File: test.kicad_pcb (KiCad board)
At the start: 2 copper layers, 161 parts, among them Q1 T2N7002AK, Q2 T2N7002AK, SW1 SW_Push, U1 ESP32-S3-WROOM-1, U2 LD1117S33TR_SOT223, U3 SN75176AD, U4 LM321, U5 LM321

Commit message: final placement-no route
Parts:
- L1, U4, U5, c4, c5, dz1, dz2, jadc1, jadc2, ra1, ra2, ra3, ra4, ra5, ra6: moved to F.Cu
- cf1, flash1, rf1, rf2, rms1: moved to B.Cu
- moved 220in1 103.9 mm to (96.8, 97.0), turned to 180 degrees
- moved MODBUS1 42.8 mm to (6.30, 35.2), turned to -90 degrees
- moved aco2 28.8 mm to (26.5, 61.7)
- moved r18 28.8 mm to (27.8, 54.3)
- moved r20 28.8 mm to (25.2, 54.2)
- moved r22 28.8 mm to (26.3, 68.4)
- moved cr2 26.3 mm to (35.0, 56.6)
- moved cb1 22.2 mm to (50.0, 57.1)
- moved cm3 22.2 mm to (59.7, 57.4)
- moved cm1 22.2 mm to (65.7, 57.4)
- moved cm2 22.2 mm to (62.7, 57.4)
- moved cm4 22.2 mm to (56.7, 57.4)
- moved cm5 22.2 mm to (53.7, 57.4)
- moved bridge2 21.3 mm to (62.6, 66.5)
- moved rb2 21.3 mm to (49.2, 64.3)
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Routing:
- net /ESP_GPIO_0: track 66.8 -> 0.00 mm
- net MGND: track 59.4 -> 0.00 mm
- net /RS485_B: track 26.5 -> 0.00 mm
- net /RS485_AO: track 23.2 -> 0.00 mm
- net /+3.3V: track 20.4 -> 0.00 mm
- net /RS485_BO: track 20.4 -> 0.00 mm
- net Net-(mcu1-PC14): track 17.2 -> 0.00 mm
- net Net-(U1-IO3): track 17.0 -> 0.00 mm, vias 1 -> 0
- net /+M5V: track 16.6 -> 0.00 mm, vias 1 -> 0
- net /RS485_A: track 15.5 -> 0.00 mm
- net Net-(mcu1-PC13): track 14.8 -> 0.00 mm
- net Net-(mcu1-PF1): track 13.8 -> 0.00 mm
- net /ESP_EN: track 13.4 -> 0.00 mm
- net /DO4: track 13.2 -> 0.00 mm
- net /RESET: track 12.9 -> 0.00 mm, vias 1 -> 0
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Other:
- board outline added: 100 x 100 mm

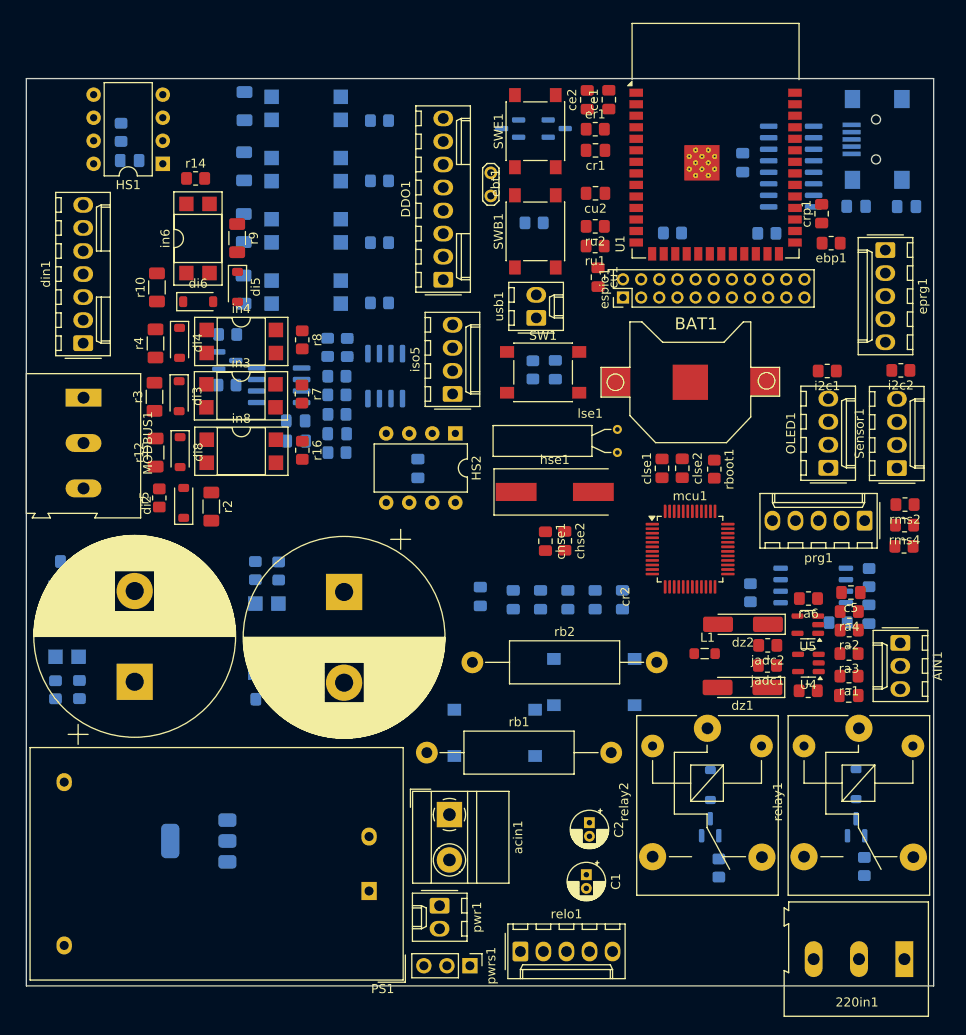
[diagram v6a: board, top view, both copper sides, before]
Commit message: except DI1-4 all other logics are ok
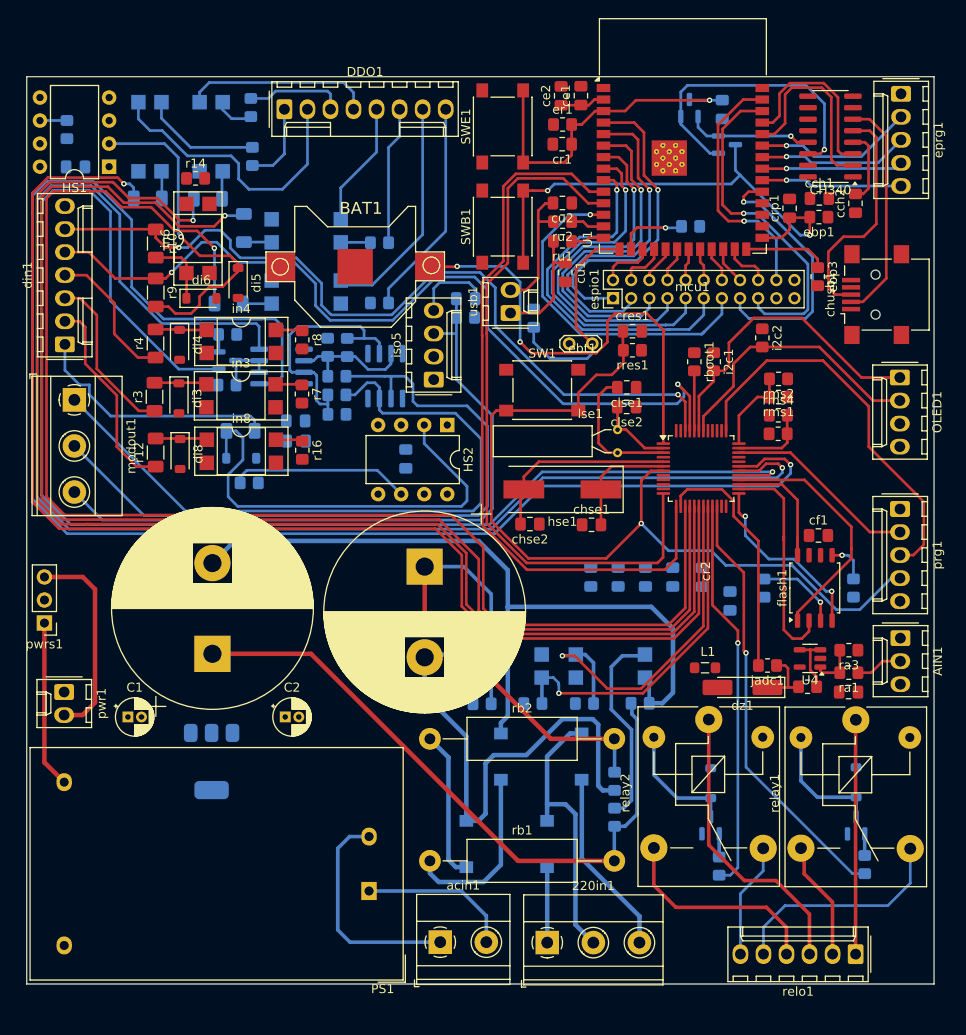
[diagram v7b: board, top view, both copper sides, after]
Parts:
- removed MODBUS1: Screw_Terminal_01x03, TerminalBlock:TerminalBlock_Altech_AK300-3_P5.00mm
- removed Sensor1: Conn_01x04_Pin, Connector_Molex:Molex_KK-254_AE-6410-04A_1x04_P2.54mm_Vertical
- removed U5: LM321, Package_TO_SOT_SMD:SOT-23-5
- removed c5: 100nF, Capacitor_SMD:C_0805_2012Metric_Pad1.18x1.45mm_HandSolder
- removed dz2: D_Zener, Diode_SMD:D_MiniMELF_Handsoldering
- removed jadc2: 0, Resistor_SMD:R_0805_2012Metric_Pad1.20x1.40mm_HandSolder
- removed ra2: 68K, Resistor_SMD:R_0805_2012Metric_Pad1.20x1.40mm_HandSolder
- removed ra4: 33K, Resistor_SMD:R_0805_2012Metric_Pad1.20x1.40mm_HandSolder
- removed ra6: 68, Resistor_SMD:R_0805_2012Metric_Pad1.20x1.40mm_HandSolder
- added modout1: Screw_Terminal_01x03, TerminalBlock_Phoenix:TerminalBlock_Phoenix_MKDS-1,5-3-5.08_1x03_P5.08mm_Horizontal, F.Cu at (5.29, 35.4)
- 220in1: footprint TerminalBlock:TerminalBlock_Altech_AK300-3_P5.00mm -> TerminalBlock_Phoenix:TerminalBlock_Phoenix_MKDS-1,5-3-5.08_1x03_P5.08mm_Horizontal
- CH340, cch1, cch2, cf1, chusb1, cres1, ebp3, flash1, rms1, rres1: moved to F.Cu
- acin1: footprint TerminalBlock_MetzConnect:TerminalBlock_MetzConnect_Type011_RT05502HBWC_1x02_P5.00mm_Horizontal -> TerminalBlock_Phoenix:TerminalBlock_Phoenix_MKDS-1,5-2-5.08_1x02_P5.08mm_Horizontal
- di2, r2, r5: moved to B.Cu
- r34, r35: value 3.3K -> 2.5K
- relo1: value Conn_01x05_Pin -> Conn_01x06_Pin; footprint Connector_Molex:Molex_KK-254_AE-6410-05A_1x05_P2.54mm_Vertical -> Connector_Molex:Molex_KK-254_AE-6410-06A_1x06_P2.54mm_Vertical
- moved r17 64.5 mm to (67.7, 68.8), turned to 180 degrees
- moved r19 60.6 mm to (64.8, 81.4)
- moved pwrs1 60.2 mm to (1.99, 60.0), turned to 180 degrees
- moved aco1 60.1 mm to (64.4, 64.8), turned to 180 degrees
- moved r21 58.9 mm to (61.5, 68.9)
- moved C1 53.4 mm to (11.2, 70.4), turned to 0 degrees
- moved pwr1 47.6 mm to (4.16, 67.6)
- moved r18 43.7 mm to (64.8, 77.5)
- moved 220in1 39.4 mm to (57.4, 95.2), turned to 0 degrees
- moved BAT1 39.1 mm to (36.2, 20.7)
- moved relo1 37.0 mm to (91.4, 96.5), turned to 180 degrees
- moved C2 35.5 mm to (28.5, 70.4), turned to 0 degrees
- moved r22 29.5 mm to (55.8, 68.9), turned to 180 degrees
- moved r20 29.0 mm to (50.2, 68.9), turned to 0 degrees
- moved cb1 27.5 mm to (77.5, 57.6)
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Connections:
- AIN1 pad 1: /AIN1 -> /+5V
- AIN1 pad 2: AGND -> /AIN1
- AIN1 pad 3: /AIN2 -> AGND
- DDO1 pad 1: /COM1 -> /COM4
- DDO1 pad 2: /DO1 -> /DO4
- DDO1 pad 3: /COM2 -> /COM3
- DDO1 pad 4: /DO2 -> /DO3
- DDO1 pad 5: /COM3 -> /DO2
- DDO1 pad 6: /DO3 -> /COM2
- DDO1 pad 7: /COM4 -> /DO1
- DDO1 pad 8: /DO4 -> /COM1
- mcu1 pad 15: /ADC_IN2 -> /MDO1
- mcu1 pad 16: unconnected-(mcu1-PA6-Pad16) -> /MDO2
- mcu1 pad 17: unconnected-(mcu1-PA7-Pad17) -> /MDO3
- mcu1 pad 18: unconnected-(mcu1-PB0-Pad18) -> /MDO4
- mcu1 pad 19: unconnected-(mcu1-PB1-Pad19) -> /D220_IN1
- mcu1 pad 20: unconnected-(mcu1-PB2-Pad20) -> /D220_IN2
- mcu1 pad 21: unconnected-(mcu1-PB10-Pad21) -> /rlo2
- mcu1 pad 22: unconnected-(mcu1-PB11-Pad22) -> /rlo1
- mcu1 pad 29: unconnected-(mcu1-PA8-Pad29) -> /RS_SEL
- mcu1 pad 30: /UART1_TX -> /MCU_TX
- mcu1 pad 31: /UART1_RX -> /MCU_RX
- mcu1 pad 45: unconnected-(mcu1-PB8-Pad45) -> /DI5
- mcu1 pad 46: unconnected-(mcu1-PB9-Pad46) -> /DI6
- relay1 pad 4: /NOC -> /NOC1
- relay2 pad 4: /NOC -> /NOC2
- relo1 pad 1: /RELOUT11 -> /RELOUT12
- relo1 pad 2: /RELOUT12 -> /RELOUT11
- relo1 pad 3: /RELOUT21 -> /RELOUT22
- relo1 pad 4: /RELOUT22 -> /RELOUT21
- relo1 pad 5: /NOC -> /NOC1
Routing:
- net /MCU_RX: track 0.00 -> 177.6 mm, vias 0 -> 1
- net /MCU_TX: track 0.00 -> 163.2 mm, vias 0 -> 1
- net /RS_SEL: track 0.00 -> 154.5 mm, vias 0 -> 1
- net /MDO1: track 0.00 -> 152.6 mm, vias 0 -> 1
- net /MDO2: track 0.00 -> 151.4 mm, vias 0 -> 1
- net /MDO3: track 0.00 -> 150.2 mm, vias 0 -> 1
- net /MDO4: track 0.00 -> 143.5 mm, vias 0 -> 1
- net /RESET: track 0.00 -> 94.6 mm, vias 0 -> 1
- net /DI5: track 0.00 -> 94.0 mm, vias 0 -> 2
- net /DI6: track 0.00 -> 89.8 mm, vias 0 -> 2
- net Net-(bridge1--): track 0.00 -> 85.6 mm
- net /ESP_MCU_TX: track 0.00 -> 80.4 mm
- net /RS485_AO: track 0.00 -> 79.4 mm
- net /ESP_MCU_RX: track 0.00 -> 78.6 mm
- net /RS485_BO: track 0.00 -> 76.8 mm
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
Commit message: all done except gnds and vccs
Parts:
- added Ds1: SS34, Diode_SMD:D_SMA, B.Cu at (29.2, 89.4)
- added L24: L, Inductor_THT:L_Radial_D9.5mm_P5.00mm_Fastron_07HVP, F.Cu at (41.6, 62.8)
- added U5: LM2576HVS-5, Package_TO_SOT_SMD:TO-263-5_TabPin3, B.Cu at (14.9, 93.2)
- added crs1: C_Polarized, Capacitor_THT:CP_Radial_D10.0mm_P3.80mm, F.Cu at (18.8, 67.6)
- added crs2: C_Polarized, Capacitor_THT:CP_Radial_D10.0mm_P3.80mm, F.Cu at (8.41, 61.5)
- PS1: value HLK-5M05 -> HLK-5M24
- cb1: moved to F.Cu
- cr2, cr3: footprint Capacitor_THT:CP_Radial_D22.0mm_P10.00mm_SnapIn -> Capacitor_THT:CP_Radial_D10.0mm_P3.80mm
- moved cb1 26.9 mm to (69.0, 32.1), turned to 180 degrees
- moved cr2 14.2 mm to (31.0, 59.8)
- moved U2 9.84 mm to (12.2, 80.7)
- moved cr3 5.27 mm to (20.5, 58.1)
- moved i2c1 3.28 mm to (74.6, 28.2), turned to 0 degrees
- moved cm7 2.58 mm to (39.3, 41.3), turned to 180 degrees
- moved dr2 2.20 mm to (76.8, 79.3), turned to 180 degrees
- moved out4 1.25 mm to (13.3, 5.19)
- moved ebp2 1.13 mm to (74.3, 16.3)
- moved cm6 0.75 mm to (4.67, 9.72)
- moved iso1 0.74 mm to (39.9, 32.1)
- moved r26 0.65 mm to (34.2, 37.7)
- moved C2 0.52 mm to (28.1, 70.2)
- moved rres1 0.37 mm to (66.7, 29.6)
- moved cres1 0.36 mm to (66.7, 27.5)
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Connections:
- dr1 pad 1: /+5V -> /+24V
- dr2 pad 1: /+5V -> /+24V
- mcu1 pad 38: unconnected-(mcu1-PA15-Pad38) -> /D24_IN1
- mcu1 pad 39: unconnected-(mcu1-PB3-Pad39) -> /D24_IN4
- mcu1 pad 40: unconnected-(mcu1-PB4-Pad40) -> /D24_IN3
- mcu1 pad 41: unconnected-(mcu1-PB5-Pad41) -> /D24_IN2
- mcu1 pad 45: /DI5 -> /D05_IN6
- mcu1 pad 46: /DI6 -> /D05_IN5
- pwrs1 pad 2: /+5V -> /+24V
- relay1 pad 5: /+5V -> /+24V
- relay2 pad 5: /+5V -> /+24V
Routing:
- net /+24V: track 0.00 -> 213.1 mm
- net /D24_IN4: track 2.95 -> 111.9 mm, vias 0 -> 2
- net /D24_IN3: track 2.94 -> 108.7 mm, vias 0 -> 2
- net /D24_IN2: track 2.98 -> 108.6 mm, vias 0 -> 2
- net /D05_IN5: track 2.97 -> 102.6 mm, vias 0 -> 1
- net /D05_IN6: track 0.00 -> 83.3 mm, vias 0 -> 2
- net /DI5: track 94.0 -> 11.2 mm, vias 2 -> 0
- net /DI6: track 89.8 -> 10.0 mm, vias 2 -> 0
- net /D24_IN1: track 19.8 -> 97.3 mm, vias 0 -> 2
- net Net-(Ds1-K): track 0.00 -> 38.2 mm
- net /+M5V: track 8.64 -> 25.3 mm, vias 0 -> 1
- net Net-(bridge2--): track 56.8 -> 70.5 mm
- net Net-(cr2-Pad1): track 56.1 -> 47.0 mm, vias 0 -> 1
- net MGND: track 75.0 -> 82.8 mm
- net Net-(cr3-Pad1): track 72.6 -> 79.3 mm
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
